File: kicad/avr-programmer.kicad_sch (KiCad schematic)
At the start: 14 parts, among them J1 Conn_02x14_Counter_Clockwise, J3 Conn_02x04_Counter_Clockwise, U1 ATmega328-P, U2 ATtiny85-20P, Y1 Crystal 16Mhz

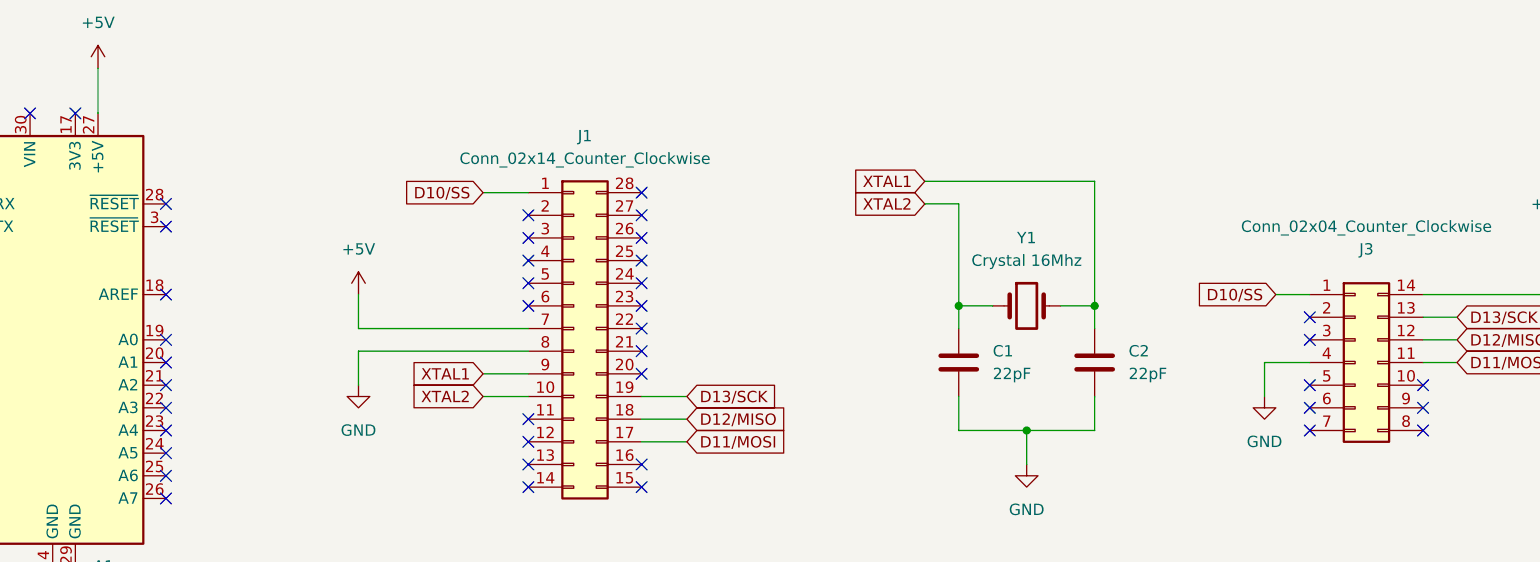
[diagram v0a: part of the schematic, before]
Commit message: bugfix: add a capacitor to prevent programmer from resetting
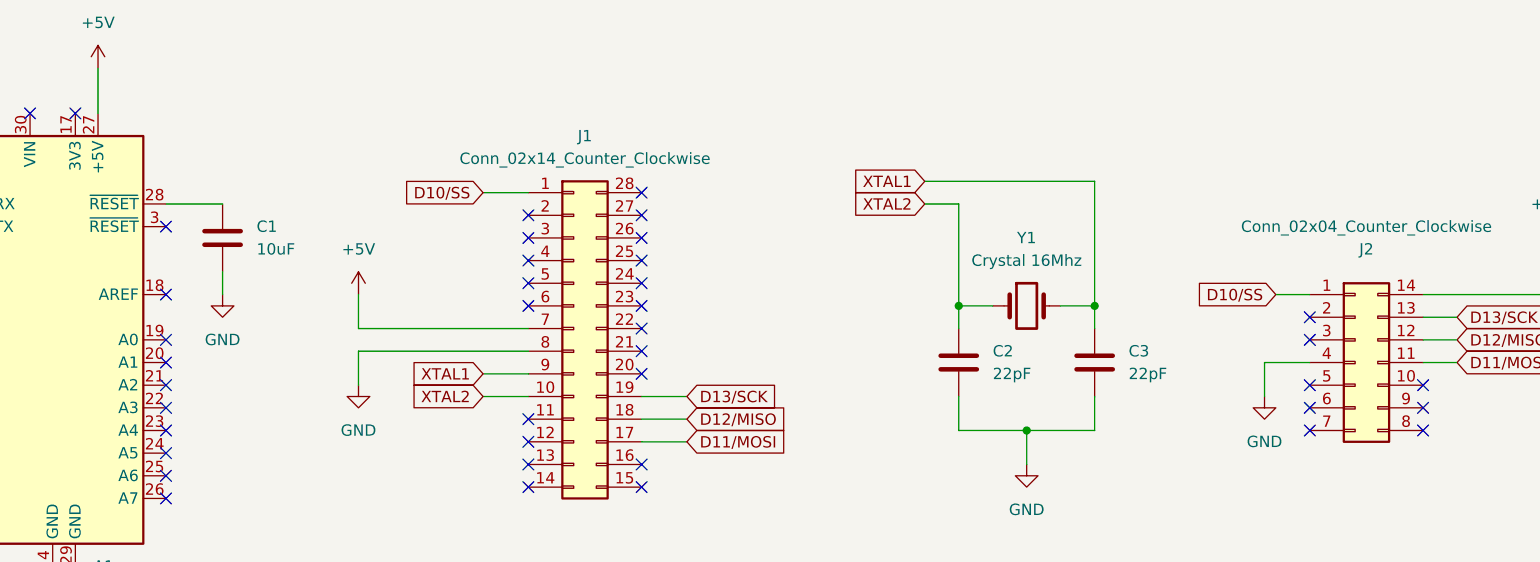
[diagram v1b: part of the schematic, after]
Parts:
- added C1: 10uF, Capacitor_THT:C_Disc_D4.3mm_W1.9mm_P5.00mm, symbol Device:C
- renumbered C1 to C2, C2 to C3, J3 to J2
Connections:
- net GND: now also C1.2
- net at A1.28 (~{RESET}): now also C1.1
- no-connect marks 73 -> 72
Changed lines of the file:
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@@
   (no_connect (at 90.17 59.69))
   (no_connect (at 90.17 62.23))
-  (no_connect (at 115.57 46.99))
   (no_connect (at 115.57 49.53))
   (no_connect (at 115.57 57.15))
@@
     (stroke (width 0) (type default) (color 0 0 0 0))
   )
+  (wire (pts (xy 121.92 54.61) (xy 121.92 57.15))
+    (stroke (width 0) (type default) (color 0 0 0 0))
+  )
   (wire (pts (xy 107.95 31.75) (xy 107.95 36.83))
     (stroke (width 0) (type default) (color 0 0 0 0))
@@
   )
   (wire (pts (xy 151.13 68.58) (xy 156.21 68.58))
+    (stroke (width 0) (type default) (color 0 0 0 0))
+  )
+  (wire (pts (xy 115.57 46.99) (xy 121.92 46.99))
     (stroke (width 0) (type default) (color 0 0 0 0))
   )
@@
     (pin "8")
   )
+  (symbol (lib_id "power:GND") (at 121.92 57.15 0) (unit 1)
+    (in_bom yes) (on_board yes) (fields_autoplaced)
+    (property "Reference" "#PWR04" (id 0) (at 121.92 63.5 0)
+      (effects (font (size 1.27 1.27)) hide)
+    )
+    (property "Value" "GND" (id 1) (at 121.92 62.23 0))
+    (property "Footprint" "" (id 2) (at 121.92 57.15 0)
+      (effects (font (size 1.27 1.27)) hide)
+    )
+    (property "Datasheet" "" (id 3) (at 121.92 57.15 0)
+      (effects (font (size 1.27 1.27)) hide)
+    )
+    (pin "1")
+  )
   (symbol (lib_id "Device:R") (at 52.07 73.66 90) (unit 1)
     (in_bom yes) (on_board yes) (fields_autoplaced)
@@
   (symbol (lib_id "Connector_Generic:Conn_02x07_Counter_Clockwise") (at 248.92 64.77 0) (unit 1)
     (in_bom yes) (on_board yes)
-    (property "Reference" "J3" (id 0) (at 250.19 52.07 0))
+    (property "Reference" "J2" (id 0) (at 250.19 52.07 0))
     (property "Value" "Conn_02x04_Counter_Clockwise" (id 1) (at 250.19 49.53 0))
     (property "Footprint" "Socket:DIP_Socket-14_W4.3_W5.08_W7.62_W10.16_W10.9_3M_214-3339-00-0602J" (id 2) (at 248.92 64.77 0)
@@
   (symbol (lib_id "power:+5V") (at 270.51 52.07 0) (unit 1)
     (in_bom yes) (on_board yes) (fields_autoplaced)
-    (property "Reference" "#PWR010" (id 0) (at 270.51 55.88 0)
+    (property "Reference" "#PWR09" (id 0) (at 270.51 55.88 0)
       (effects (font (size 1.27 1.27)) hide)
     )
@@
   (symbol (lib_id "Device:C") (at 204.47 64.77 0) (unit 1)
     (in_bom yes) (on_board yes) (fields_autoplaced)
-    (property "Reference" "C1" (id 0) (at 208.28 63.4999 0)
+    (property "Reference" "C2" (id 0) (at 208.28 63.4999 0)
       (effects (font (size 1.27 1.27)) (justify left))
     )
@@
   (symbol (lib_id "power:+5V") (at 137.16 57.15 0) (unit 1)
     (in_bom yes) (on_board yes) (fields_autoplaced)
-    (property "Reference" "#PWR04" (id 0) (at 137.16 60.96 0)
+    (property "Reference" "#PWR05" (id 0) (at 137.16 60.96 0)
       (effects (font (size 1.27 1.27)) hide)
     )
@@
   (symbol (lib_id "power:GND") (at 137.16 67.31 0) (unit 1)
     (in_bom yes) (on_board yes) (fields_autoplaced)
-    (property "Reference" "#PWR05" (id 0) (at 137.16 73.66 0)
+    (property "Reference" "#PWR06" (id 0) (at 137.16 73.66 0)
       (effects (font (size 1.27 1.27)) hide)
     )
@@
   (symbol (lib_id "power:PWR_FLAG") (at 86.36 87.63 0) (unit 1)
     (in_bom yes) (on_board yes) (fields_autoplaced)
-    (property "Reference" "#FLG0101" (id 0) (at 86.36 85.725 0)
+    (property "Reference" "#FLG01" (id 0) (at 86.36 85.725 0)
       (effects (font (size 1.27 1.27)) hide)
     )
@@
   (symbol (lib_id "Device:C") (at 219.71 64.77 0) (unit 1)
     (in_bom yes) (on_board yes) (fields_autoplaced)
-    (property "Reference" "C2" (id 0) (at 223.52 63.4999 0)
+    (property "Reference" "C3" (id 0) (at 223.52 63.4999 0)
       (effects (font (size 1.27 1.27)) (justify left))
     )
@@
   (symbol (lib_id "power:GND") (at 238.76 68.58 0) (unit 1)
     (in_bom yes) (on_board yes)
-    (property "Reference" "#PWR09" (id 0) (at 238.76 74.93 0)
+    (property "Reference" "#PWR08" (id 0) (at 238.76 74.93 0)
       (effects (font (size 1.27 1.27)) hide)
     )
@@
     (pin "9")
   )
+  (symbol (lib_id "Device:C") (at 121.92 50.8 0) (unit 1)
+    (in_bom yes) (on_board yes) (fields_autoplaced)
+    (property "Reference" "C1" (id 0) (at 125.73 49.5299 0)
+      (effects (font (size 1.27 1.27)) (justify left))
+    )
+    (property "Value" "10uF" (id 1) (at 125.73 52.0699 0)
+      (effects (font (size 1.27 1.27)) (justify left))
+    )
+    (property "Footprint" "Capacitor_THT:C_Disc_D4.3mm_W1.9mm_P5.00mm" (id 2) (at 122.8852 54.61 0)
+      (effects (font (size 1.27 1.27)) hide)
+    )
+    (property "Datasheet" "~" (id 3) (at 121.92 50.8 0)
+      (effects (font (size 1.27 1.27)) hide)
+    )
+    (pin "1")
+    (pin "2")
+  )
   (symbol (lib_id "power:GND") (at 212.09 76.2 0) (unit 1)
     (in_bom yes) (on_board yes) (fields_autoplaced)
-    (property "Reference" "#PWR06" (id 0) (at 212.09 82.55 0)
+    (property "Reference" "#PWR07" (id 0) (at 212.09 82.55 0)
       (effects (font (size 1.27 1.27)) hide)
     )
@@
   (symbol_instances
     (path "/7e62e98f-b065-4dad-9edb-e87e88fd5d8f"
-      (reference "#FLG0101") (unit 1) (value "PWR_FLAG") (footprint "")
+      (reference "#FLG01") (unit 1) (value "PWR_FLAG") (footprint "")
     )
     (path "/61312efa-db4f-4817-af08-f2f6dd902e17"
@@
       (reference "#PWR03") (unit 1) (value "+5V") (footprint "")
     )
+    (path "/19e8ef54-ad69-4bdf-802d-af0bb9e91ca7"
+      (reference "#PWR04") (unit 1) (value "GND") (footprint "")
+    )
     (path "/6735d3e0-c721-4dbd-983f-c352755f3300"
-      (reference "#PWR04") (unit 1) (value "+5V") (footprint "")
+      (reference "#PWR05") (unit 1) (value "+5V") (footprint "")
     )
     (path "/6dbfc9b6-54da-43fa-a786-9fc4675ded56"
-      (reference "#PWR05") (unit 1) (value "GND") (footprint "")
+      (reference "#PWR06") (unit 1) (value "GND") (footprint "")
     )
     (path "/f04171de-8ca4-48a4-859b-7fa9636ce0b2"
-      (reference "#PWR06") (unit 1) (value "GND") (footprint "")
+      (reference "#PWR07") (unit 1) (value "GND") (footprint "")
     )
     (path "/c94c0daf-4e67-4c65-84ff-e840ddad32ce"
-      (reference "#PWR09") (unit 1) (value "GND") (footprint "")
+      (reference "#PWR08") (unit 1) (value "GND") (footprint "")
     )
     (path "/37b1ab36-7249-4561-aaf4-fb866d6c78b5"
-      (reference "#PWR010") (unit 1) (value "+5V") (footprint "")
+      (reference "#PWR09") (unit 1) (value "+5V") (footprint "")
     )
     (path "/ce26bc7a-ed9a-4ccc-b76c-8a49da970019"
       (reference "A1") (unit 1) (value "Arduino_Nano_v3.x") (footprint "Module:Arduino_Nano")
     )
+    (path "/eaee294a-2a1a-4de0-9271-2dbb3d197d0b"
+      (reference "C1") (unit 1) (value "10uF") (footprint "Capacitor_THT:C_Disc_D4.3mm_W1.9mm_P5.00mm")
+    )
     (path "/45c86363-17f1-41a4-8b06-56a24b68611c"
-      (reference "C1") (unit 1) (value "22pF") (footprint "Capacitor_THT:C_Disc_D4.7mm_W2.5mm_P5.00mm")
+      (reference "C2") (unit 1) (value "22pF") (footprint "Capacitor_THT:C_Disc_D4.7mm_W2.5mm_P5.00mm")
     )
     (path "/981c1b15-3d98-465b-aa86-6f575f5dfc26"
-      (reference "C2") (unit 1) (value "22pF") (footprint "Capacitor_THT:C_Disc_D4.7mm_W2.5mm_P5.00mm")
+      (reference "C3") (unit 1) (value "22pF") (footprint "Capacitor_THT:C_Disc_D4.7mm_W2.5mm_P5.00mm")
     )
     (path "/1cb82eb7-0ff8-4a42-aa69-c14d9618af80"
@@
     )
     (path "/31963ce4-bff1-43b8-8499-4758f02f2dbd"
-      (reference "J3") (unit 1) (value "Conn_02x04_Counter_Clockwise") (footprint "Socket:DIP_Socket-14_W4.3_W5.08_W7.62_W10.16_W10.9_3M_214-3339-00-0602J")
+      (reference "J2") (unit 1) (value "Conn_02x04_Counter_Clockwise") (footprint "Socket:DIP_Socket-14_W4.3_W5.08_W7.62_W10.16_W10.9_3M_214-3339-00-0602J")
     )
     (path "/b306ddcb-8058-4ecc-ad01-875f82bcf388"
